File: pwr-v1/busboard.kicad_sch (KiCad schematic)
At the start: 46 parts

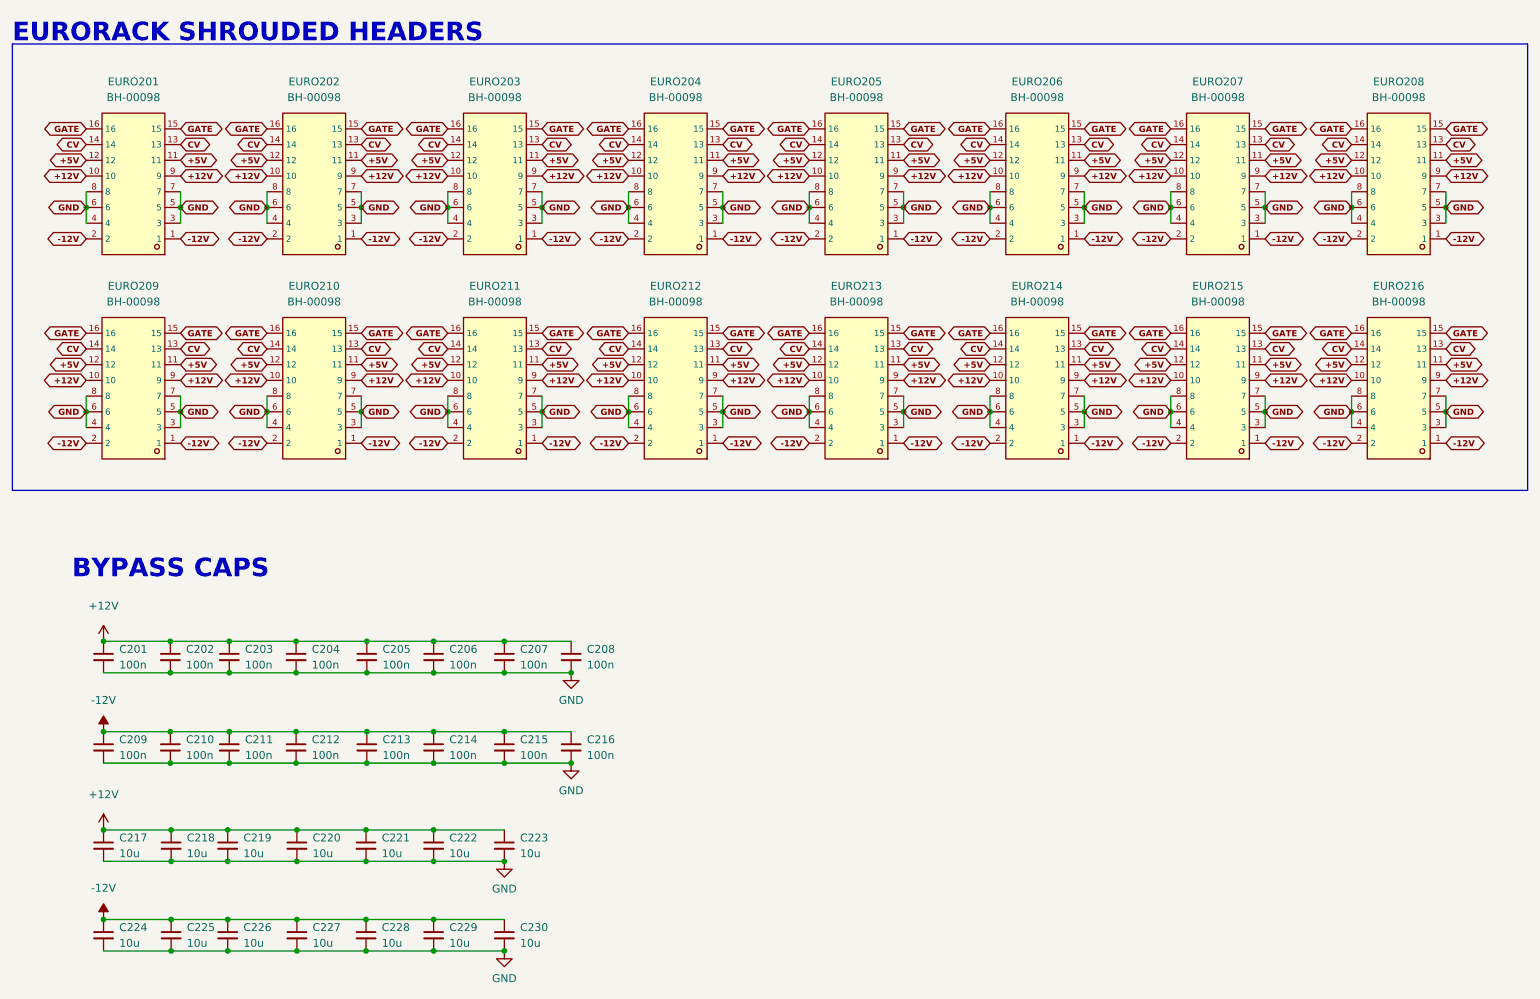
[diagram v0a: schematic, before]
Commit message: Fix bad edgecuts
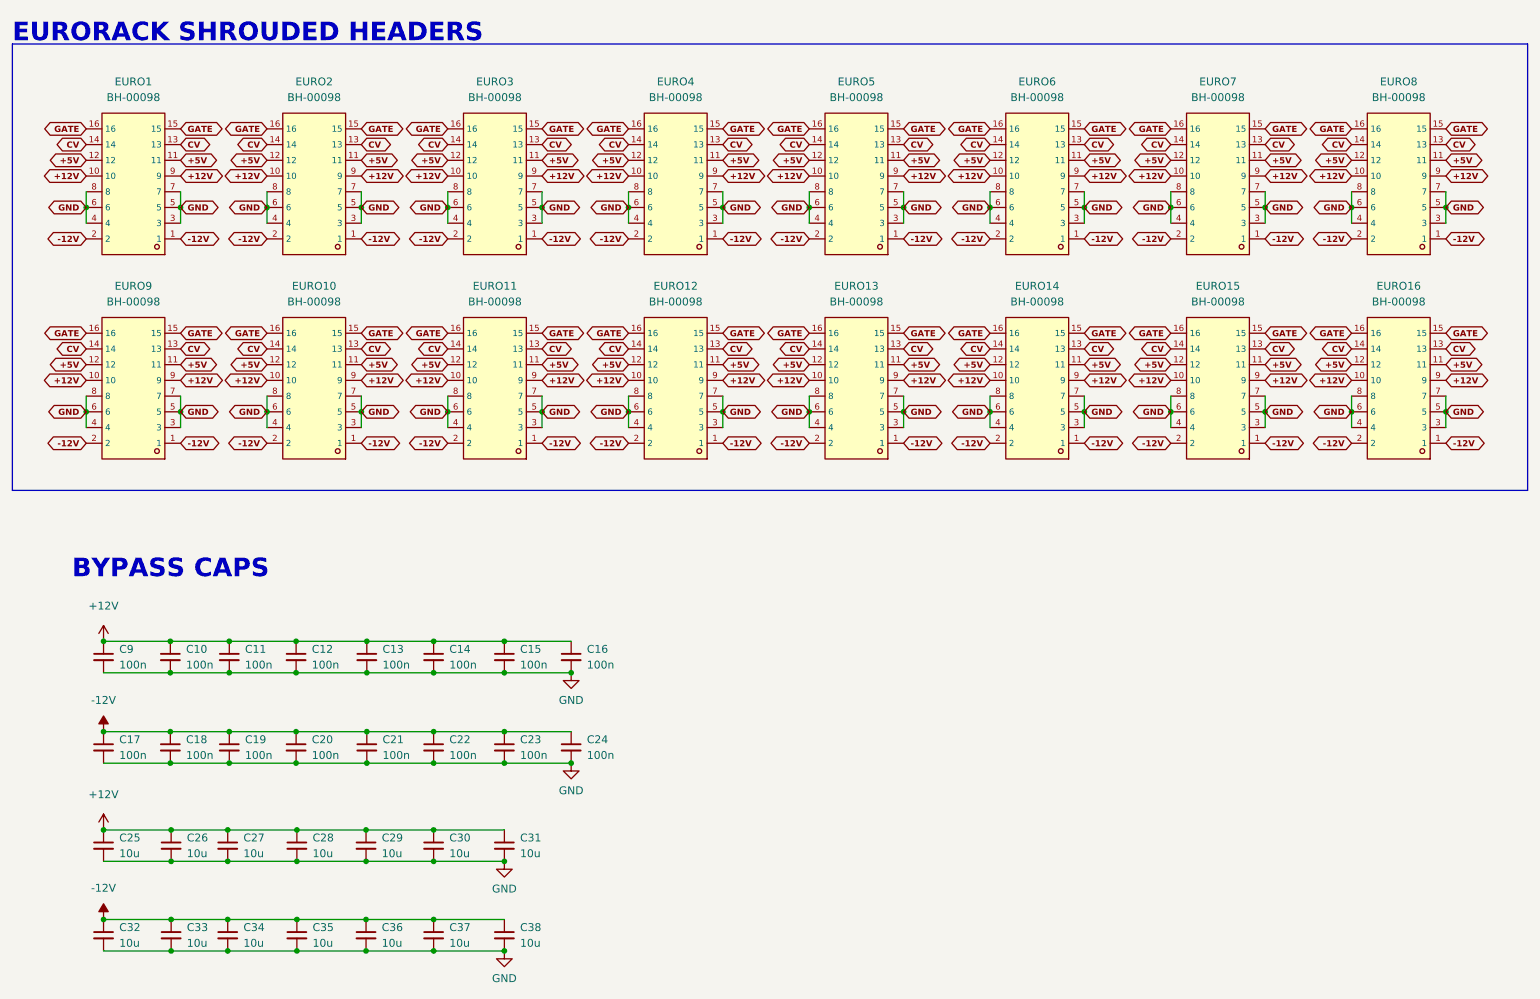
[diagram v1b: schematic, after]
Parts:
- renumbered C202 to C10, C203 to C11, C204 to C12, C205 to C13, C206 to C14, C207 to C15, C208 to C16, C209 to C17, C210 to C18, C211 to C19, C212 to C20, C213 to C21, C214 to C22, C215 to C23, C216 to C24, C217 to C25, C218 to C26, C219 to C27, C220 to C28, C221 to C29, C222 to C30, C223 to C31, C224 to C32, C225 to C33, C226 to C34, C227 to C35, C228 to C36, C229 to C37, C230 to C38, C201 to C9, EURO201 to EURO1, EURO210 to EURO10, EURO211 to EURO11, EURO212 to EURO12, EURO213 to EURO13, EURO214 to EURO14, EURO215 to EURO15, EURO216 to EURO16, EURO202 to EURO2, EURO203 to EURO3, EURO204 to EURO4, EURO205 to EURO5, EURO206 to EURO6, EURO207 to EURO7, EURO208 to EURO8, EURO209 to EURO9
